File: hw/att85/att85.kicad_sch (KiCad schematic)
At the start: 38 parts, among them J101 Barrel_Jack_Switch, J102 Screw_Terminal_01x03, J103 AVR-ISP-6, J104 Conn_01x02, J105 Conn_01x02, Q101 BC817, Q102 BC817, SW101 SW_Push, SW102 SW_Push, SW103 SW_Push, SW104 SW_Push, SW105 SW_Push, SW106 SW_Push, U101 ATtiny85-20P, U102 MT3608-MODULE

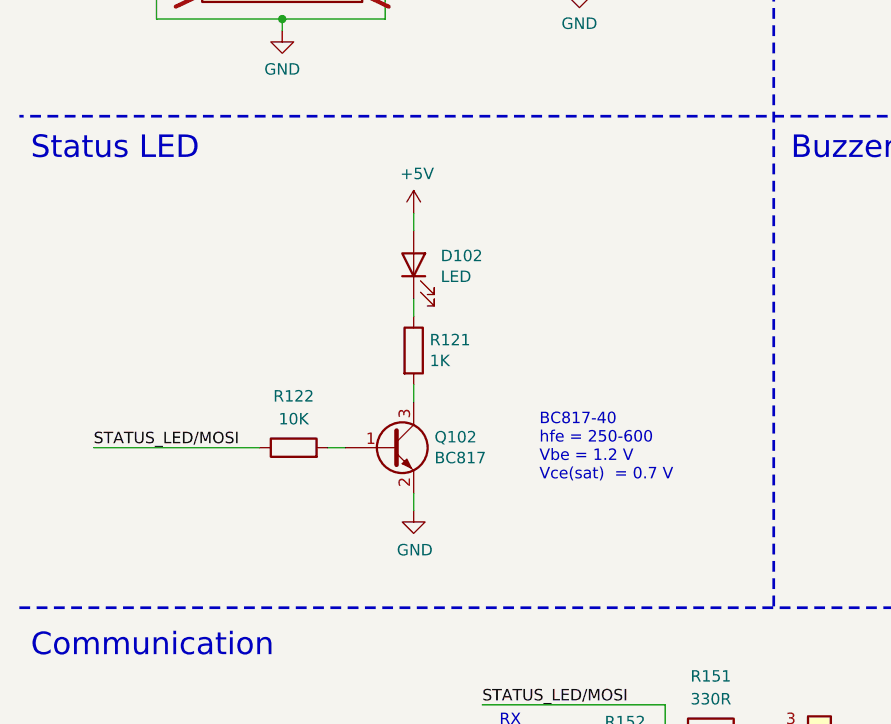
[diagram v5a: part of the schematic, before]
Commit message: chore(hw): switch status LED for WS2812B
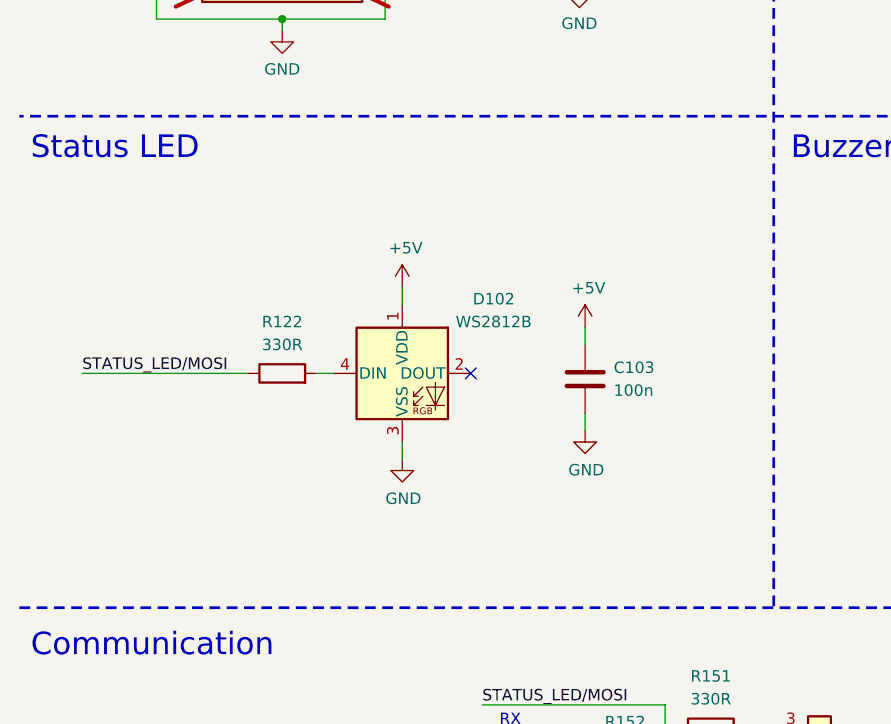
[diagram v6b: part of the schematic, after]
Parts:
- removed D102: LED, LED_SMD:LED_0805_2012Metric_Pad1.15x1.40mm_HandSolder, symbol Device:LED
- removed Q102: BC817, Package_TO_SOT_SMD:SOT-23_Handsoldering, symbol Device:Q_NPN_BEC
- removed R121: 1K, Resistor_SMD:R_0805_2012Metric_Pad1.20x1.40mm_HandSolder, symbol Device:R
- added C103: 100n, Capacitor_SMD:C_0805_2012Metric_Pad1.18x1.45mm_HandSolder, symbol Device:C
- added D102: WS2812B, LED_SMD:LED_WS2812B_PLCC4_5.0x5.0mm_P3.2mm, symbol LED:WS2812B
- R122: value 10K -> 330R
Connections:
- net +5V: now also C103.1, D102.1 (VDD)
- net GND: now also C103.2, D102.3 (VSS)
- net at R122.2: now also D102.4 (DIN)
- no-connect marks 1 -> 2
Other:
- note removed: "BC817-40 hfe = 250-600 Vbe = 1.2 V Vce(sat) = 0.7 V"
- moved on the sheet: R122

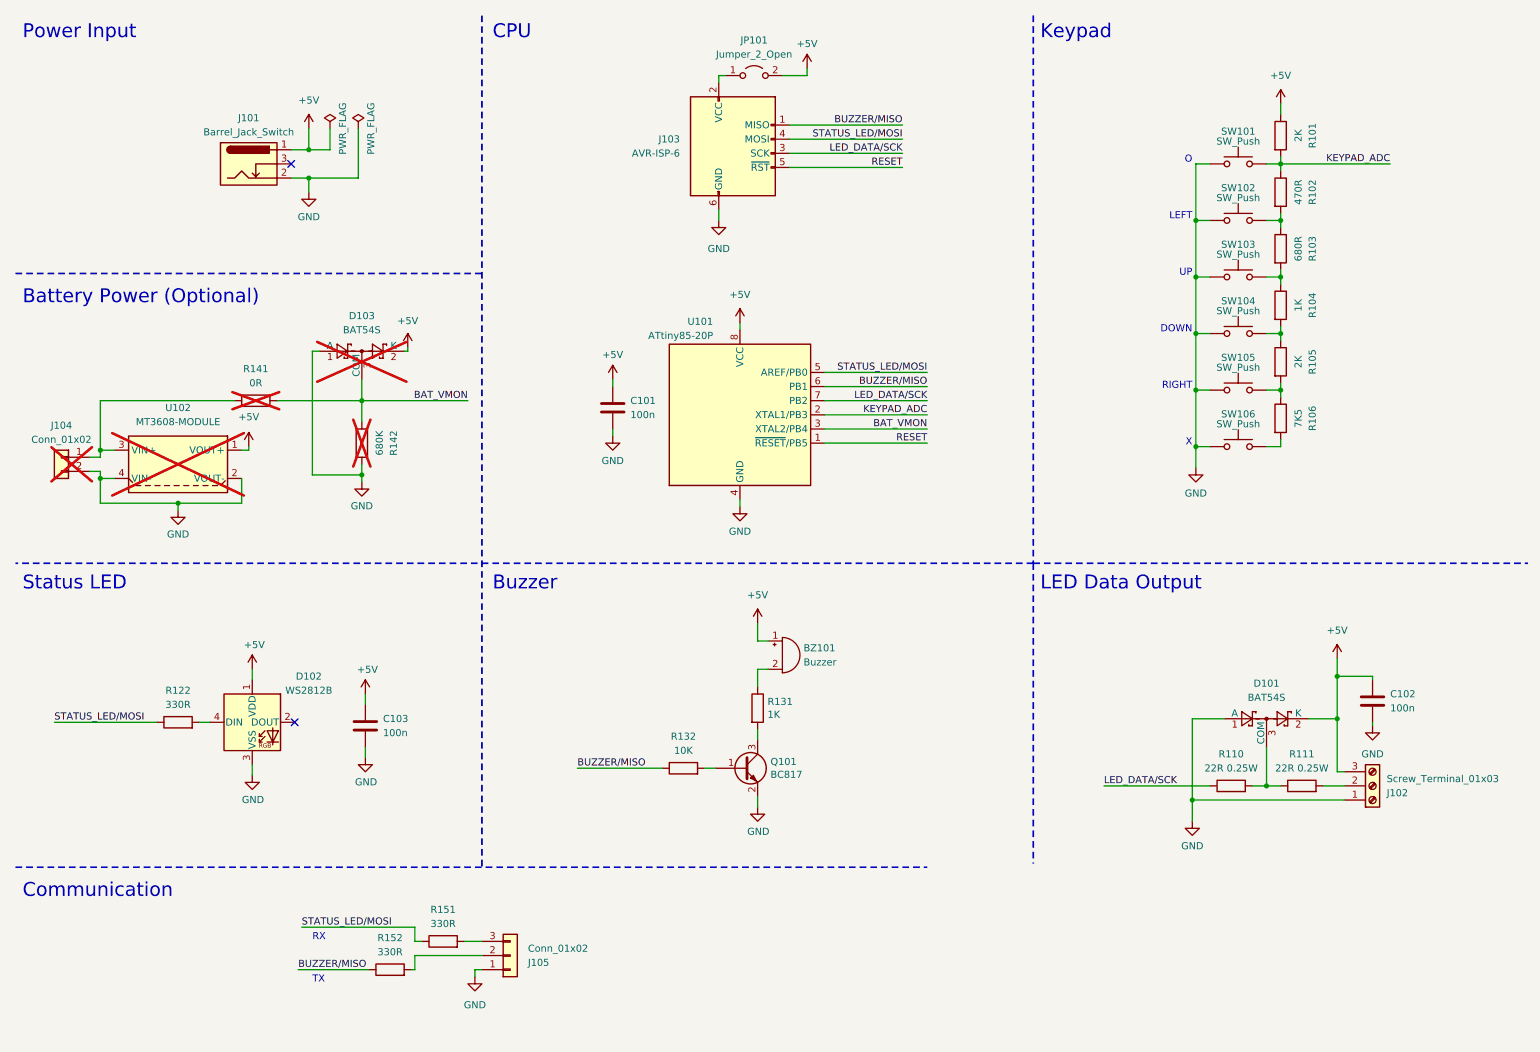
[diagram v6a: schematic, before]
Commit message: feat(hw): add IR receiver
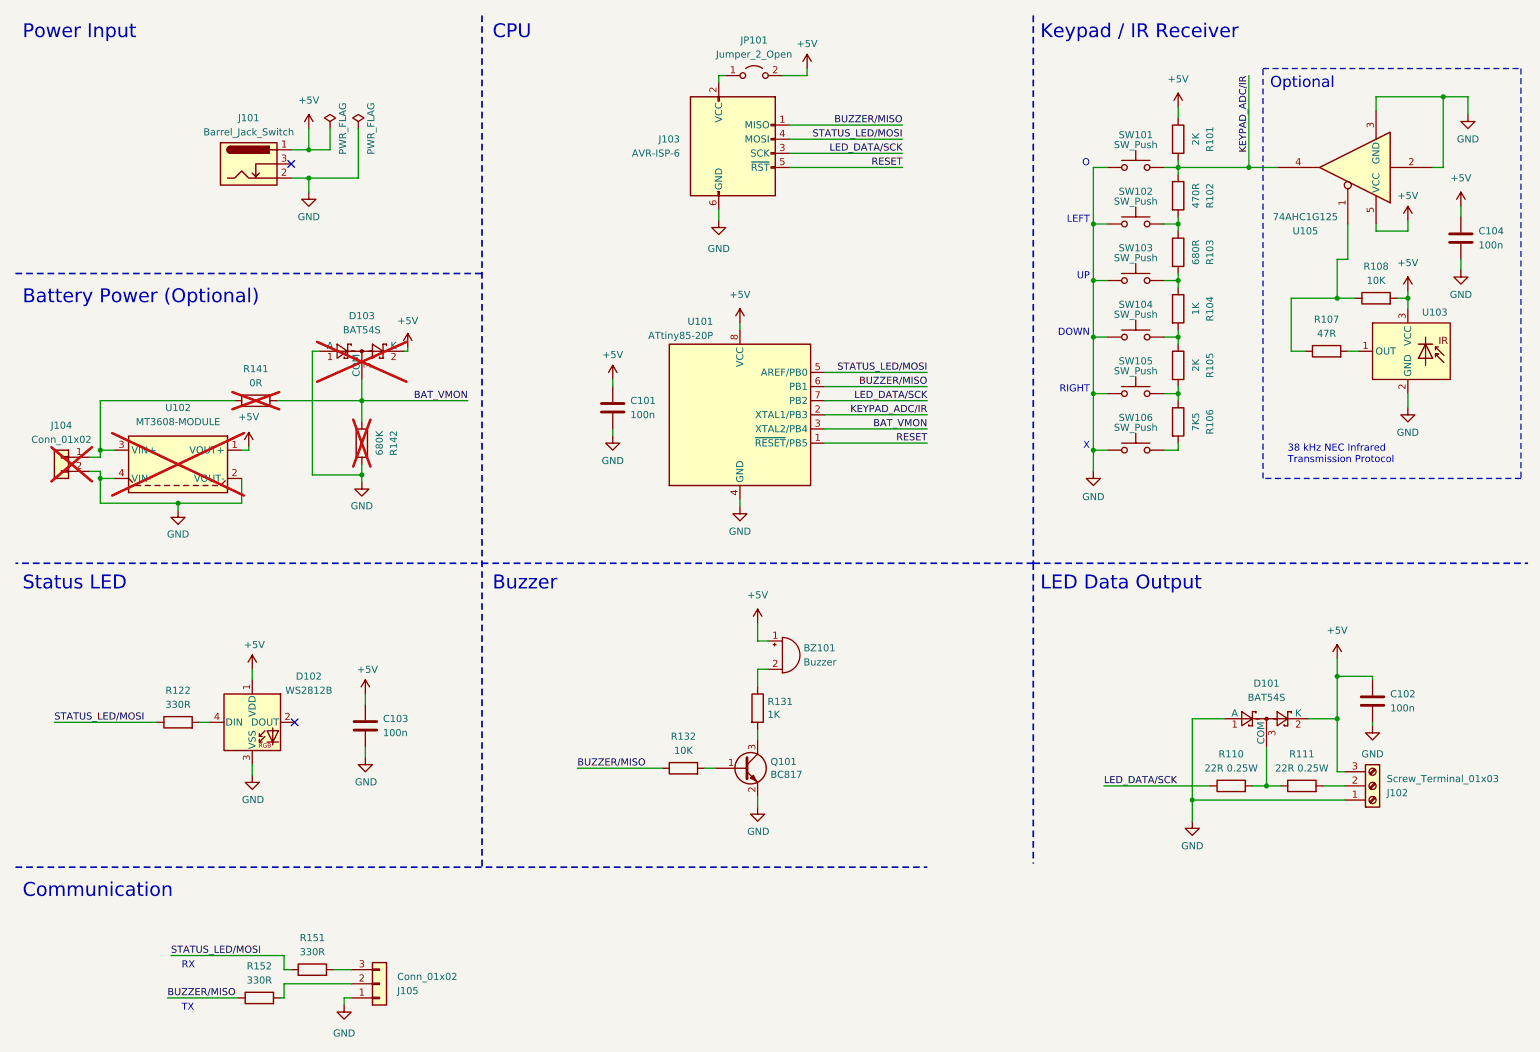
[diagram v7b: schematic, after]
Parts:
- added C104: 100n, Capacitor_SMD:C_0805_2012Metric_Pad1.18x1.45mm_HandSolder, symbol Device:C
- added R107: 47R, Resistor_SMD:R_0805_2012Metric_Pad1.20x1.40mm_HandSolder, symbol Device:R
- added R108: 10K, Resistor_SMD:R_0805_2012Metric_Pad1.20x1.40mm_HandSolder, symbol Device:R
- added U103: ~, Connector_PinSocket_2.54mm:PinSocket_1x03_P2.54mm_Vertical, symbol project-specific:IR_Receiver
- added U105: 74AHC1G125, Package_TO_SOT_SMD:SOT-23-5_HandSoldering, symbol 74xGxx:74AHC1G125
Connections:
- net +5V: now also C104.1, R108.2, U103.3 (VCC), U105.5 (VCC)
- net GND: now also C104.2, U103.2 (GND), U105.2, U105.3 (GND)
- net KEYPAD_ADC renamed KEYPAD_ADC/IR
- net KEYPAD_ADC/IR: now also U105.4
- new net: R107.1, R108.1, U105.1
- new net: R107.2, U103.1 (OUT)
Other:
- note added: "38 kHz NEC Infrared Transmission Protocol"
- note added: "Keypad / IR Receiver"
- note added: "Optional"
- note removed: "Keypad"
- moved on the sheet: J105, R101, R102, R103, R104, R105, R106, R151, R152, SW101, SW102, SW103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

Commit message: chore(hw): add notes
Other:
- note added: "The buffer is preventing pull-up resistor embedded inside IR receiver form affecting the resistor divider."
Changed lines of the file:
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@@
     (stroke (width 0.3) (type dash))
   )
-  (rectangle (start 236.855 22.225) (end 283.21 95.885)
+  (rectangle (start 236.855 22.225) (end 283.21 92.075)
     (stroke (width 0.2) (type dash))
     (fill (type none))
@@
   (text "RIGHT" (at 205.74 80.645 0)
     (effects (font (size 1.27 1.27)) (justify right bottom))
+  )
+  (text "The buffer is\npreventing pull-up\nresistor embedded\ninside IR receiver form\naffecting the resistor\ndivider."
+    (at 238.125 90.805 0)
+    (effects (font (size 1.27 1.27)) (justify left bottom))
   )
   (text "Battery Power (Optional)" (at 13.97 64.77 0)
@@
     (effects (font (size 1.27 1.27)) (justify right bottom))
   )
-  (text "38 kHz NEC Infrared\nTransmission Protocol" (at 241.3 93.345 0)
+  (text "38 kHz NEC\nInfrared\nTransmission\nProtocol" (at 267.335 86.995 0)
     (effects (font (size 1.27 1.27)) (justify left bottom))
   )
